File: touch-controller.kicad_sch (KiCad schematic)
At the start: 76 parts, among them J1 IR_DATA, J2 USB_C_Receptacle_USB2.0_16P, J3 IR_LED, J4 LED, K1 Conn_01x01, K10 Conn_01x01, K11 Conn_01x01, K12 Conn_01x01, K13 Conn_01x01, K14 Conn_01x01, K15 Conn_01x01, K16 Conn_01x01, K17 Conn_01x01, K18 Conn_01x01, K19 Conn_01x01, K2 Conn_01x01, K20 Conn_01x01, K21 Conn_01x01, K22 Conn_01x01, K23 Conn_01x01, K24 Conn_01x01, K25 Conn_01x01, K26 Conn_01x01, K27 Conn_01x01, K28 Conn_01x01, K29 Conn_01x01, K3 Conn_01x01, K30 Conn_01x01, K31 Conn_01x01, K32 Conn_01x01, K4 Conn_01x01, K5 Conn_01x01, K6 Conn_01x01, K7 Conn_01x01, K8 Conn_01x01, K9 Conn_01x01, Q1 BC818, Q2 BC818, SW1 FSM2JSMAATR, SW2 FSM2JSMAATR, U1 CH340C, U2 TVS0500DRVR, U3 TLV1117-33, U4 ESP32-S3-WROOM-1, U5 CAP1188-1-CP-TR, U6 CAP1188-1-CP-TR, U7 CAP1188-1-CP-TR, U8 CAP1188-1-CP-TR, U9 TPD2EUSB30DRTR

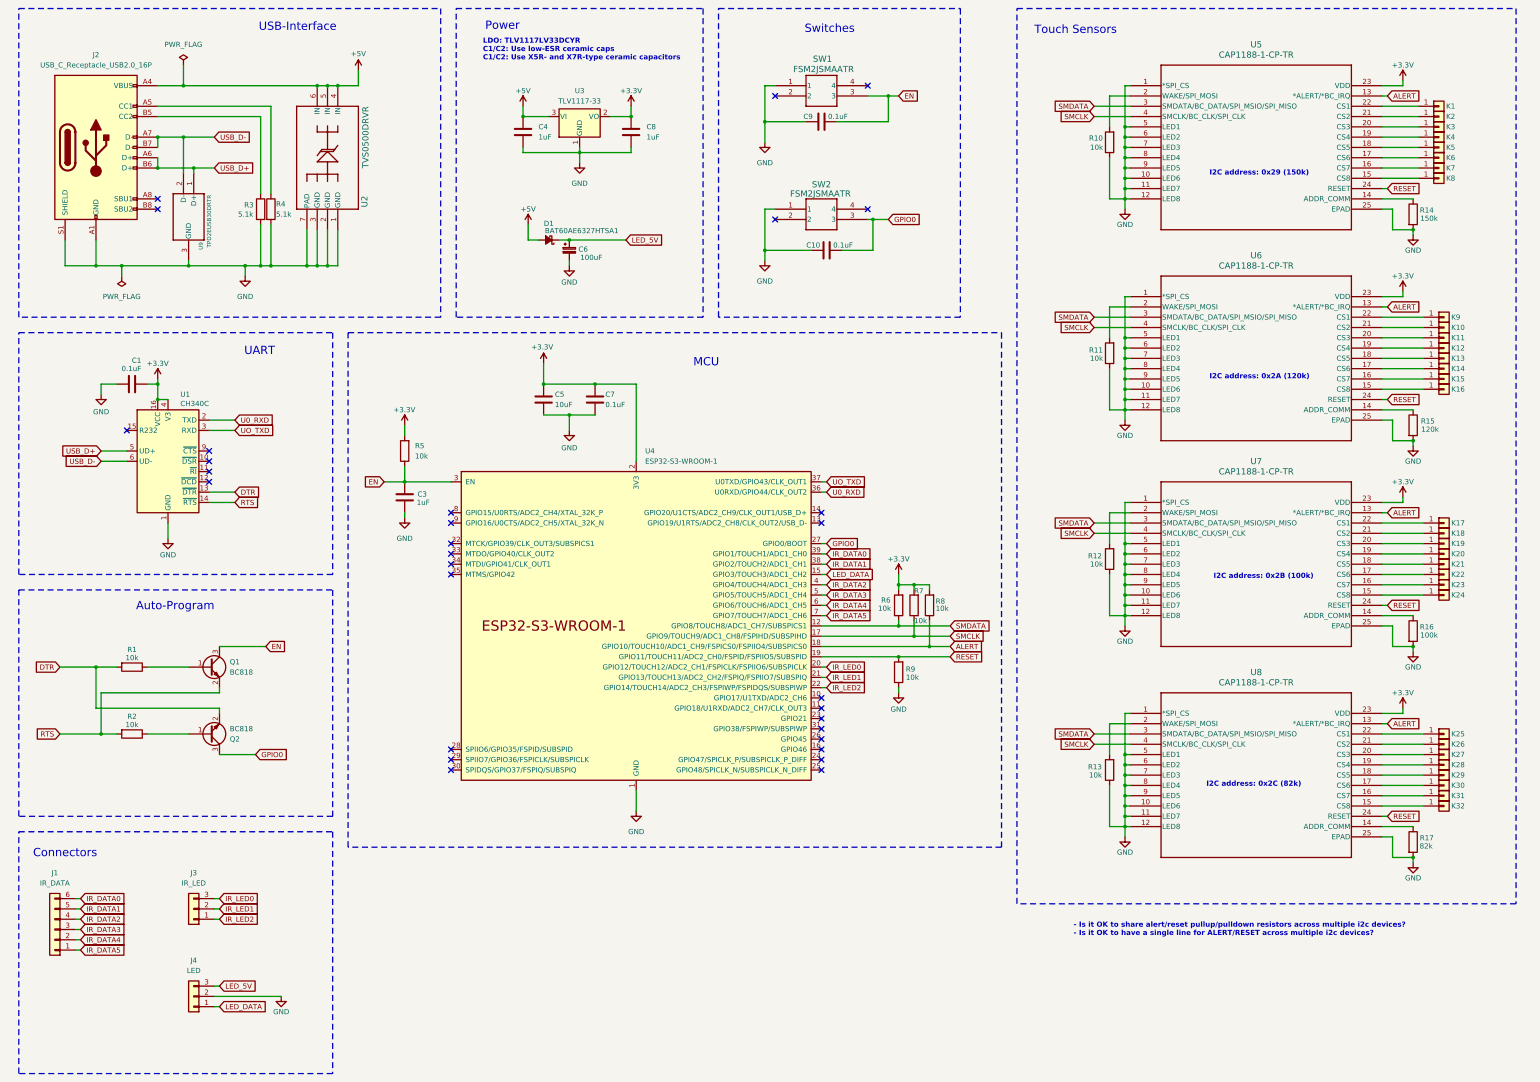
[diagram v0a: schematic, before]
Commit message: Add ToF sensor & other changes (pcb broken)
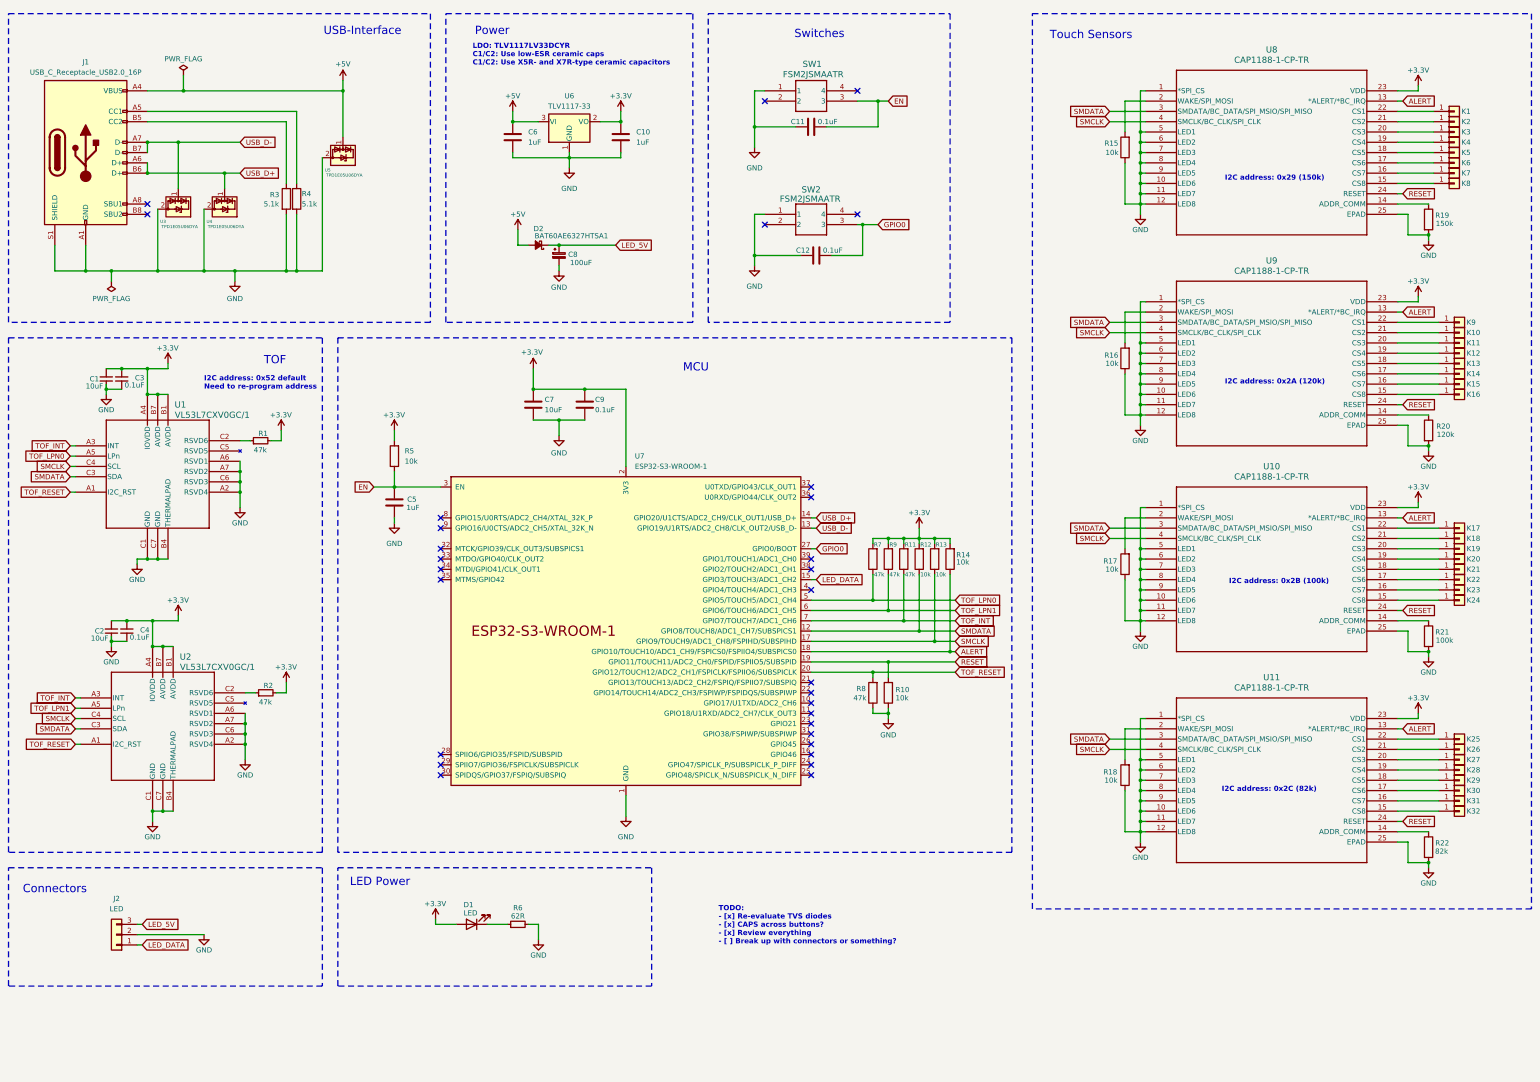
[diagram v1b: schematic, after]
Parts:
- removed C1: 0.1uF, Capacitor_SMD:C_0805_2012Metric_Pad1.18x1.45mm_HandSolder, symbol Device:C
- removed J1: IR_DATA, Connector_PinHeader_2.54mm:PinHeader_1x06_P2.54mm_Horizontal, symbol Connector_Generic:Conn_01x06
- removed J3: IR_LED, Connector_PinHeader_2.54mm:PinHeader_1x03_P2.54mm_Horizontal, symbol Connector_Generic:Conn_01x03
- removed Q1, Q2: BC818, Package_TO_SOT_SMD:SOT-23, symbol Transistor_BJT:BC818
- removed R1, R2: 10k, Resistor_SMD:R_0805_2012Metric_Pad1.20x1.40mm_HandSolder, symbol Device:R
- removed U1: CH340C, Package_SO:SOIC-16_3.9x9.9mm_P1.27mm, symbol Interface_USB:CH340C
- removed U2: TVS0500DRVR, TVS0500DRVR:DRV0006A, symbol TVS0500DRVR:TVS0500DRVR
- removed U9: TPD2EUSB30DRTR, DRT0003A, symbol TPD2EUSB30DRTR:TPD2EUSB30DRTR
- added C1, C2: 10uF, Capacitor_SMD:C_0805_2012Metric_Pad1.18x1.45mm_HandSolder, symbol Device:C_Small
- added C3, C4: 0.1uF, Capacitor_SMD:C_0805_2012Metric_Pad1.18x1.45mm_HandSolder, symbol Device:C_Small
- added D1: LED, LED_SMD:LED_0805_2012Metric_Pad1.15x1.40mm_HandSolder, symbol Device:LED
- added R1, R2: 47k, Resistor_SMD:R_0805_2012Metric_Pad1.20x1.40mm_HandSolder, symbol Device:R_Small
- added R11, R7, R8, R9: 47k, Resistor_SMD:R_0805_2012Metric_Pad1.20x1.40mm_HandSolder, symbol Device:R
- added R6: 62R, Resistor_SMD:R_0805_2012Metric_Pad1.20x1.40mm_HandSolder, symbol Device:R_Small
- added U1, U2: VL53L7CXV0GC/1, VL53L7CXV0GC-1:LGA16_OPTICAL-LINER_STM, symbol VL53L7CXV0GC-1:VL53L7CXV0GC_1
- added U3, U4, U5: TPD1E05U06DYA, Diode_SMD:D_SOD-523, symbol Power_Protection:TPD1E05U06DYA
- C8: renamed from C6; footprint Capacitor_THT:CP_Radial_D6.3mm_P2.50mm -> Capacitor_SMD:CP_Elec_6.3x5.8
- renumbered C8 to C10, C9 to C11, C10 to C12, C3 to C5, C4 to C6, C5 to C7, C7 to C9, D1 to D2, J2 to J1, J4 to J2, R9 to R10, R6 to R12, R7 to R13, R8 to R14, R10 to R15, R11 to R16, R12 to R17, R13 to R18, R14 to R19, R15 to R20, R16 to R21, R17 to R22, U7 to U10, U8 to U11, U3 to U6, U4 to U7, U5 to U8, U6 to U9
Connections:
- net +3.3V: now also C1.2, C2.2, C3.2, C4.2, D1.2 (A), R1.2, R11.2, R2.2, R7.2, R9.2, U1.A4 (IOVDD), U1.B1 (AVDD), U1.B7 (AVDD), U2.A4 (IOVDD), U2.B1 (AVDD), U2.B7 (AVDD)
- net +5V: now also U5.1 (I/O)
- net GND: now also C1.1, C2.1, C3.1, C4.1, R6.2, R8.1, U1.A2 (RSVD4), U1.A6 (RSVD1), U1.A7 (RSVD2), U1.B4 (THERMALPAD), U1.C1 (GND), U1.C6 (RSVD3), U1.C7 (GND), U2.A2 (RSVD4), U2.A6 (RSVD1), U2.A7 (RSVD2), U2.B4 (THERMALPAD), U2.C1 (GND), U2.C6 (RSVD3), U2.C7 (GND), U3.2 (GND), U4.2 (GND), U5.2 (GND)
- net SMCLK: now also U1.C4 (SCL), U2.C4 (SCL)
- net SMDATA: now also U1.C3 (SDA), U2.C3 (SDA)
- net USB_D+: now also U7.14 (GPIO20/U1CTS/ADC2_CH9/CLK_OUT1/USB_D+), U4.1 (I/O)
- net USB_D-: now also U7.13 (GPIO19/U1RTS/ADC2_CH8/CLK_OUT2/USB_D-), U3.1 (I/O)
- net IR_DATA0: no longer names the net of U7.39 (GPIO1/TOUCH1/ADC1_CH0)
- net IR_DATA1: no longer names the net of U7.38 (GPIO2/TOUCH2/ADC1_CH1)
- net IR_DATA2: no longer names the net of U7.4 (GPIO4/TOUCH4/ADC1_CH3)
- net IR_DATA3 renamed TOF_LPN0
- net TOF_LPN0: now also R7.1, U1.A5 (LPn)
- net IR_DATA4 renamed TOF_LPN1
- net TOF_LPN1: now also R9.1, U2.A5 (LPn)
- net IR_DATA5 renamed TOF_INT
- net TOF_INT: now also R11.1, U1.A3 (INT), U2.A3 (INT)
- net IR_LED0 renamed TOF_RESET
- net TOF_RESET: now also R8.2, U1.A1 (I2C_RST), U2.A1 (I2C_RST)
- net IR_LED1: no longer names the net of U7.21 (GPIO13/TOUCH13/ADC2_CH2/FSPIQ/FSPIIO7/SUBSPIQ)
- net IR_LED2: no longer names the net of U7.22 (GPIO14/TOUCH14/ADC2_CH3/FSPIWP/FSPIDQS/SUBSPIWP)
- net U0_RXD: no longer names the net of U7.36 (U0RXD/GPIO44/CLK_OUT2)
- net UO_TXD: no longer names the net of U7.37 (U0TXD/GPIO43/CLK_OUT1)
- new net: D1.1 (K), R6.1
- new net: R1.1, U1.C2 (RSVD6)
- new net: R2.1, U2.C2 (RSVD6)
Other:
- note added: "I2C address: 0x52 default Need to re-program address"
- note added: "LED Power"
- note added: "TODO: - [x] Re-evaluate TVS diodes - [x] CAPS across buttons? - [x] Review everything - [ ] Break up with connectors or something?"
- note added: "TOF"
- note removed: "- Is it OK to share alert/reset pullup/pulldown resistors across multiple i2c devices? - Is it OK to have a single line for ALERT/RESET across multiple i2c devices?"
- note removed: "Auto-Program"
- note removed: "UART"
- moved on the sheet: C10, C11, C12, C5, C6, C7, C8, C9, D2, J1, J2, K1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

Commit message: Partial pcb fix
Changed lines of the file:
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@@
 	(text "TODO:\n- [x] Re-evaluate TVS diodes\n- [x] CAPS across buttons?\n- [x] Review everything\n- [ ] Break up with connectors or something?"
 		(exclude_from_sim no)
-		(at 191.77 241.554 0)
+		(at 188.976 237.998 0)
 		(effects
 			(font
